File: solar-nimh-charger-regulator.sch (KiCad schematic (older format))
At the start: 12 parts, among them J1 Conn_01x05, SW1 SW_SPST, SW2 SW_SPST, U1 TPS61070, U2 YX805

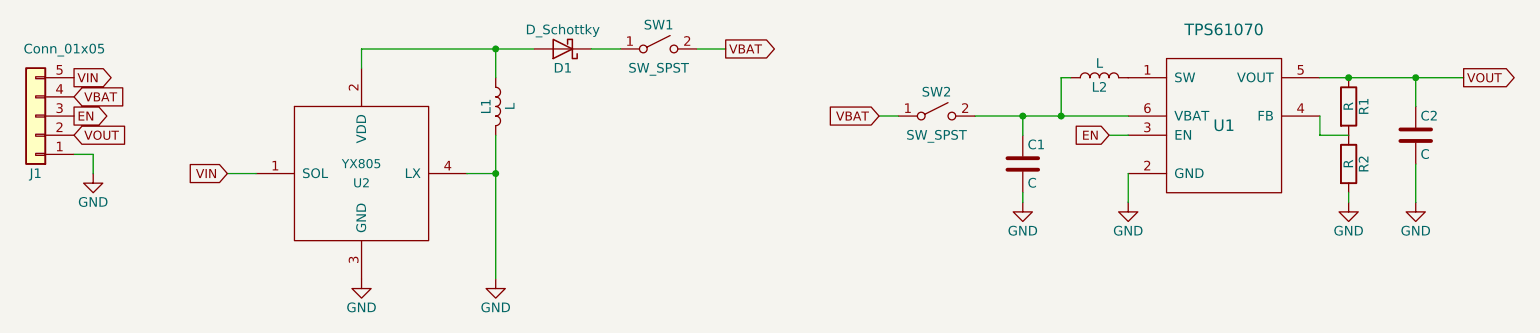
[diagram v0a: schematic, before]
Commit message: Added values to passive components
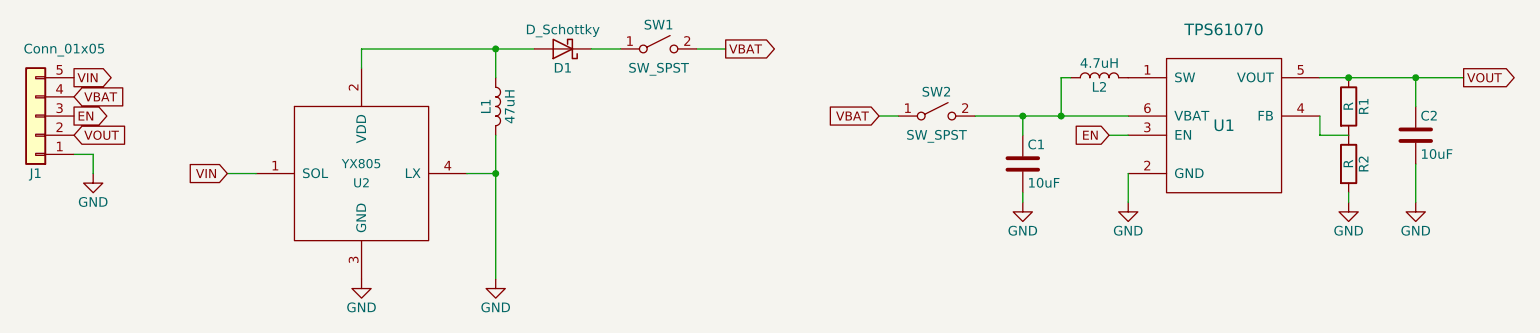
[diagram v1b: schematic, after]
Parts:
- C1, C2: value C -> 10uF
- L1: value L -> 47uH
- L2: value L -> 4.7uH
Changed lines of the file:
@@
 P 7650 3350
 F 0 "L2" V 7600 3350 50  0000 C CNN
-F 1 "L" V 7725 3350 50  0000 C CNN
+F 1 "4.7uH" V 7725 3350 50  0000 C CNN
 F 2 "Capacitors_SMD:C_0805" H 7650 3350 50  0001 C CNN
 F 3 "" H 7650 3350 50  0001 C CNN
@@
 P 7250 3800
 F 0 "C1" H 7275 3900 50  0000 L CNN
-F 1 "C" H 7275 3700 50  0000 L CNN
+F 1 "10uF" H 7275 3700 50  0000 L CNN
 F 2 "Capacitors_SMD:C_0603" H 7288 3650 50  0001 C CNN
 F 3 "" H 7250 3800 50  0001 C CNN
@@
 P 9300 3650
 F 0 "C2" H 9325 3750 50  0000 L CNN
-F 1 "C" H 9325 3550 50  0000 L CNN
+F 1 "10uF" H 9325 3550 50  0000 L CNN
 F 2 "Capacitors_SMD:C_0603" H 9338 3500 50  0001 C CNN
 F 3 "" H 9300 3650 50  0001 C CNN
@@
 P 4500 3500
 F 0 "L1" V 4450 3500 50  0000 C CNN
-F 1 "L" V 4575 3500 50  0000 C CNN
+F 1 "47uH" V 4575 3500 50  0000 C CNN
 F 2 "Capacitors_SMD:C_0805" H 4500 3500 50  0001 C CNN
 F 3 "" H 4500 3500 50  0001 C CNN

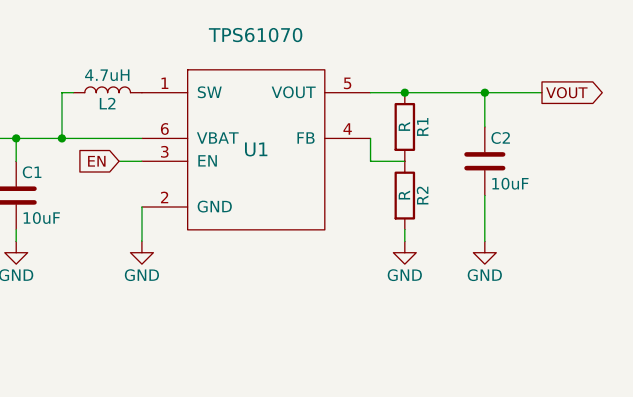
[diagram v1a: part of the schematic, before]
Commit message: Voltage divider values
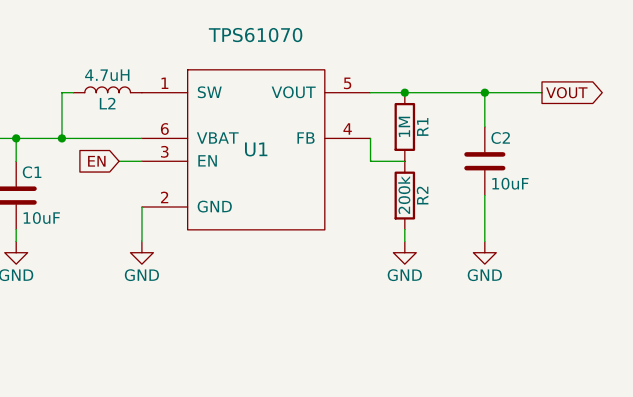
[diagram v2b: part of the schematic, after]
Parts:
- R1: value R -> 1M
- R2: value R -> 200k
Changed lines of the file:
@@
 P 8950 3500
 F 0 "R1" V 9030 3500 50  0000 C CNN
-F 1 "R" V 8950 3500 50  0000 C CNN
+F 1 "1M" V 8950 3500 50  0000 C CNN
 F 2 "Capacitors_SMD:C_0603" V 8880 3500 50  0001 C CNN
 F 3 "" H 8950 3500 50  0001 C CNN
@@
 P 8950 3800
 F 0 "R2" V 9030 3800 50  0000 C CNN
-F 1 "R" V 8950 3800 50  0000 C CNN
+F 1 "200k" V 8950 3800 50  0000 C CNN
 F 2 "Capacitors_SMD:C_0603" V 8880 3800 50  0001 C CNN
 F 3 "" H 8950 3800 50  0001 C CNN
